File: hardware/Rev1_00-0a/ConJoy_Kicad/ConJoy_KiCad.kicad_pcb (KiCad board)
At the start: 2 copper layers, 40 x 59 mm, 20 parts, among them J1 SFV5R-2STBE1HLF, J11 5051102291, J8 0532610271, J9 0532610271

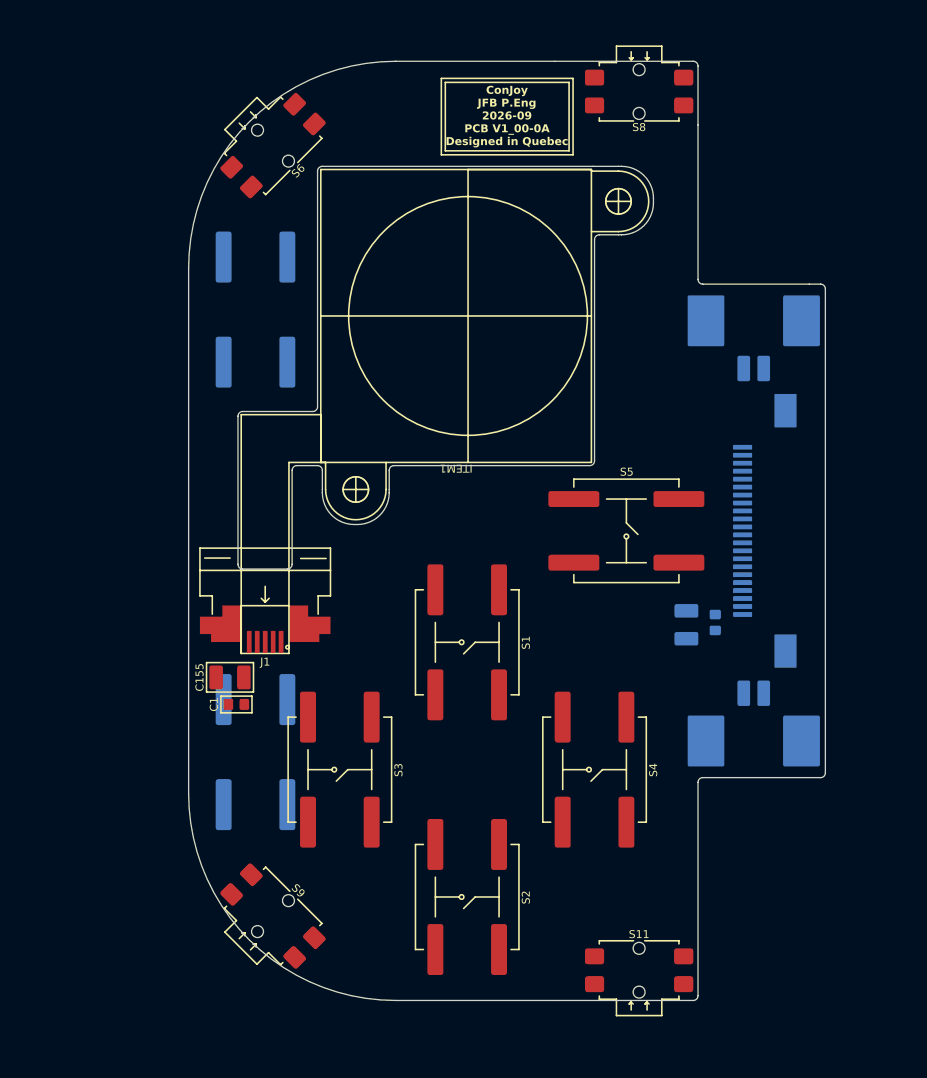
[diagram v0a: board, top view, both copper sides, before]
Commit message: Switch speaker pinout following footprint and 3d model review Add mounting holes
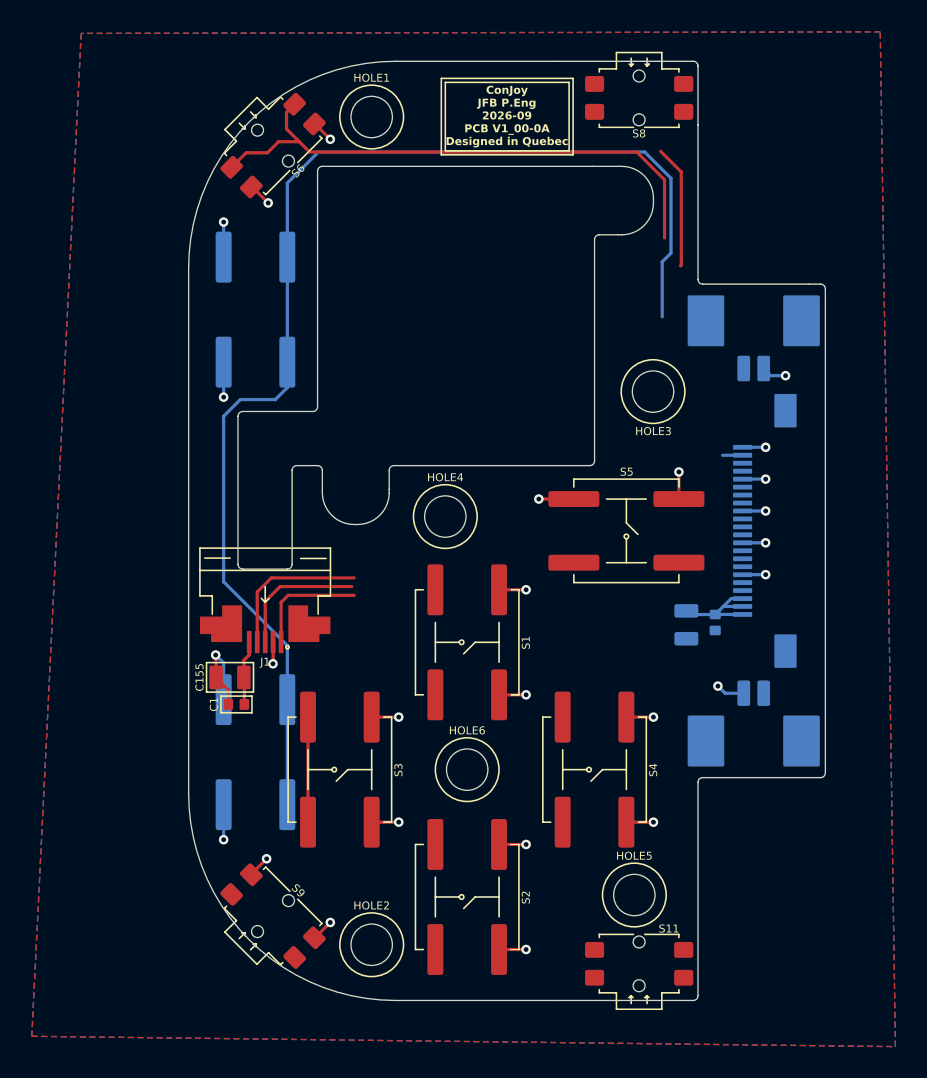
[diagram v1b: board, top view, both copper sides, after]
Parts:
- removed ITEM1: HallPi PCB FP, footprint:JoyCon_HallEffect_TMR
- added HOLE1: ~, footprint:NPTH_M2, F.Cu at (131.5, 95.5)
- added HOLE2: ~, footprint:NPTH_M2, F.Cu at (131.5, 147.5)
- added HOLE3: ~, footprint:NPTH_M2, F.Cu at (149.2, 112.8)
- added HOLE4: ~, footprint:NPTH_M2, F.Cu at (136.1, 120.6)
- added HOLE5: ~, footprint:NPTH_M2, F.Cu at (148.0, 144.4)
- added HOLE6: ~, footprint:NPTH_M2, F.Cu at (137.5, 136.5)
- moved S11 0.40 mm to (148.3, 148.7)
- moved S8 0.40 mm to (148.3, 94.3)
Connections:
- J1 pad 1: /L_THUMBST_X -> /L_R_THUMBST_X
- J1 pad 3: /L_THUMBST_SW -> /L_R_THUMBST_SW
- J1 pad 4: /L_THUMBST_Y -> /L_R_THUMBST_Y
- J8 pad 1: GND -> /L_R_SPKOUT
- J8 pad 2: /L_R_SPKOUT -> GND
- J9 pad 1: GND -> /L_R_SPKOUT
- J9 pad 2: /L_R_SPKOUT -> GND
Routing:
- net /L_R_L2_TRIG: track 0.00 -> 78.2 mm
- net GND: track 0.00 -> 48.2 mm, vias 0 -> 26
- net /L_R_L1_TRIG: track 0.00 -> 35.4 mm
- net 3V3: track 0.00 -> 11.0 mm
- net /L_R_THUMBST_Y: track 0.00 -> 9.60 mm
- net /L_HOME/R_EXTRA: track 0.00 -> 9.01 mm
- net /L_R_THUMBST_SW: track 0.00 -> 8.37 mm
- net /L_R_THUMBST_X: track 0.00 -> 7.27 mm
- net /L_DPAD_LEFT/R_BTN_X: track 0.00 -> 6.60 mm
- added copper zone on B.Cu, net GND
- added copper zone on F.Cu, net GND

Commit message: ConJoy mostly ready for alpha prototype. Confirm few other potential tweaks at 3d printing
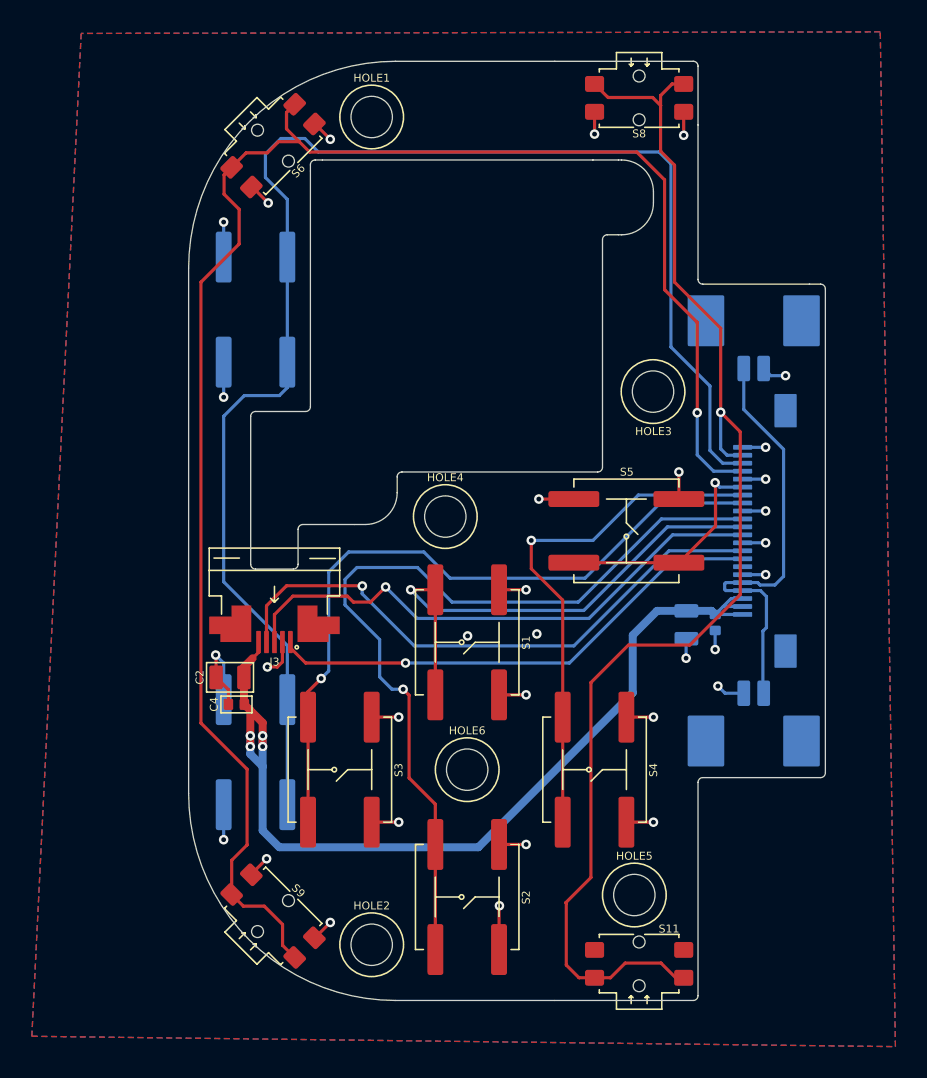
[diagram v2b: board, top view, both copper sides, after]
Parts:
- moved J3 0.58 mm to (125.4, 126.0)
- renumbered C156 to C1, C155 to C2, C2 to C3, C1 to C4, J9 to J1, J8 to J2, J1 to J3, J11 to J4
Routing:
- net /L_HOME/R_EXTRA: track 9.01 -> 82.3 mm, vias 0 -> 1
- net /L_R_L1_TRIG: track 35.4 -> 108.4 mm, vias 0 -> 1
- net /L_DPAD_DOWN/R_BTN_B: track 0.00 -> 54.4 mm, vias 0 -> 1
- net 3V3: track 11.0 -> 60.2 mm, vias 0 -> 4
- net /L_DPAD_LEFT/R_BTN_X: track 6.60 -> 45.4 mm, vias 0 -> 1
- net /L_DPAD_RIGHT/R_BTN_Y: track 0.00 -> 33.0 mm, vias 0 -> 1
- net /L_DPAD_UP/R_BTN_A: track 0.00 -> 31.7 mm, vias 0 -> 1
- net /L_R_SPKOUT: track 0.00 -> 27.5 mm
- net /L_R_THUMBST_Y: track 9.60 -> 37.0 mm, vias 0 -> 1
- net /L_R_THUMBST_SW: track 8.37 -> 35.2 mm, vias 0 -> 1
- net /L_R_THUMBST_X: track 7.27 -> 31.9 mm, vias 0 -> 1
- net /L_R_L2_TRIG: track 78.2 -> 94.0 mm
- net /L_START/R_SELECT: track 0.00 -> 14.4 mm, vias 0 -> 1
- net GND: track 48.2 -> 55.5 mm, vias 26 -> 32
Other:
- outline, holes or cut-outs redrawn

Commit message: Commit ConJoy design + output files (ready for manufacturing or REV 1.00-0A)
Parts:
- added D1: MMSZ5226B-7-F, footprint:SOD-123, B.Cu at (149.2, 128.3)
- added FID1: ~, footprint:FIDUCIAL, F.Cu at (148.3, 105.3)
- added FID2: ~, footprint:FIDUCIAL, B.Cu at (148.3, 105.3)
- added FID3: ~, footprint:FIDUCIAL, F.Cu at (129.0, 144.1)
- added FID4: ~, footprint:FIDUCIAL, B.Cu at (129.0, 144.1)
- added FID5: ~, footprint:FIDUCIAL, F.Cu at (142.7, 143.4)
- added FID6: ~, footprint:FIDUCIAL, B.Cu at (142.7, 143.4)
- HOLE1, HOLE2, HOLE3, HOLE4, HOLE5, HOLE6: moved to B.Cu
- turned HOLE1 to 180 degrees
- turned HOLE2 to 180 degrees
- turned HOLE3 to 180 degrees
- turned HOLE4 to 180 degrees
- turned HOLE5 to 180 degrees
- turned HOLE6 to 180 degrees
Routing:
- net GND: track 55.5 -> 60.3 mm, vias 32 -> 78
- net /L_R_THUMBST_Y: track 37.0 -> 36.1 mm
- net 3V3: track 60.2 -> 61.1 mm
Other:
- board text added: "PROD INFO"

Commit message: Add a lillllllll more clearance on inner cutout of ConJoy for Flat Flex cable of joystick
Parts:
- moved J3 0.51 mm to (125.3, 126.5)
- moved C2 0.30 mm to (122.6, 131.0)
- moved C4 0.30 mm to (123.0, 132.7)
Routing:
- net GND: track 60.3 -> 65.1 mm, vias 78 -> 75
- net /L_R_L1_TRIG: track 108.5 -> 112.3 mm
- net /L_R_THUMBST_X: track 31.9 -> 32.7 mm
- net /L_R_THUMBST_Y: track 36.1 -> 36.6 mm
- net /L_R_THUMBST_SW: track 35.2 -> 35.7 mm
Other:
- outline, holes or cut-outs redrawn

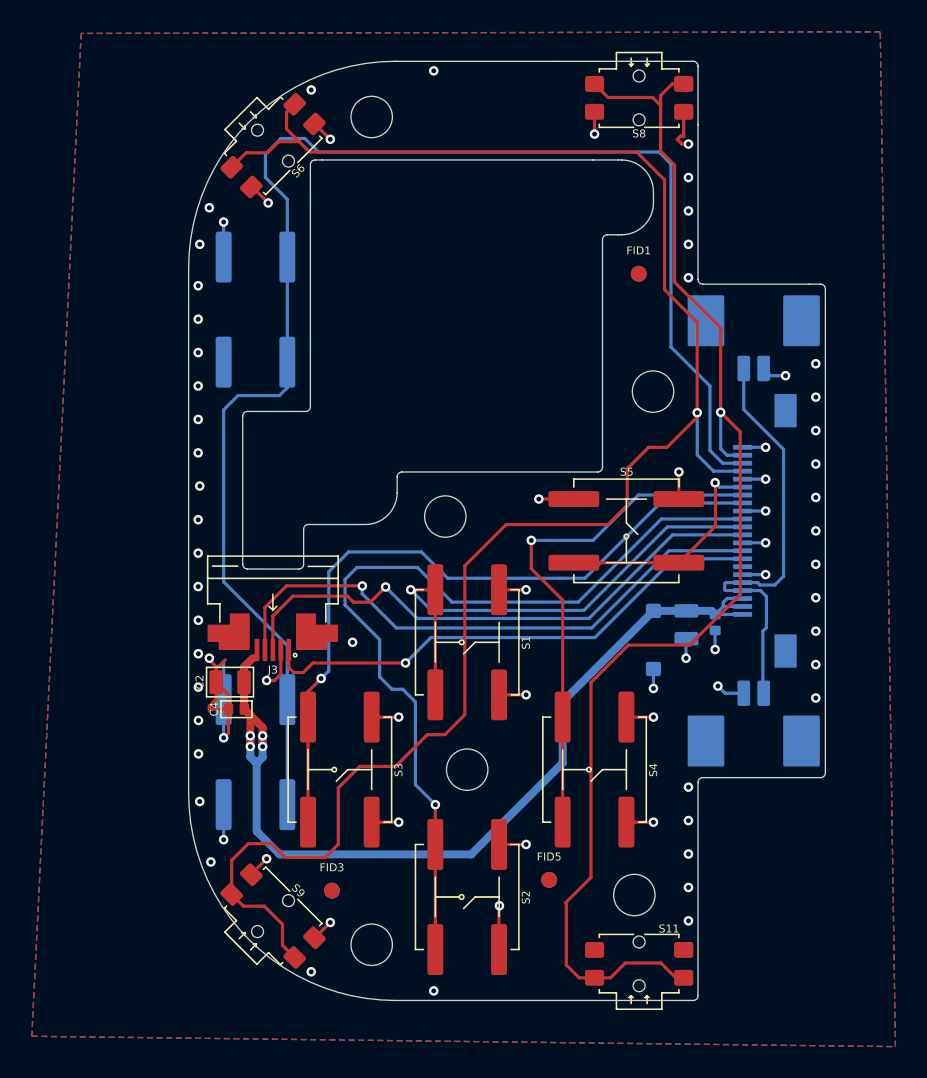
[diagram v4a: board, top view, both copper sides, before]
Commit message: Adjust mounting holes on ConJoy to ease case 3d modeling
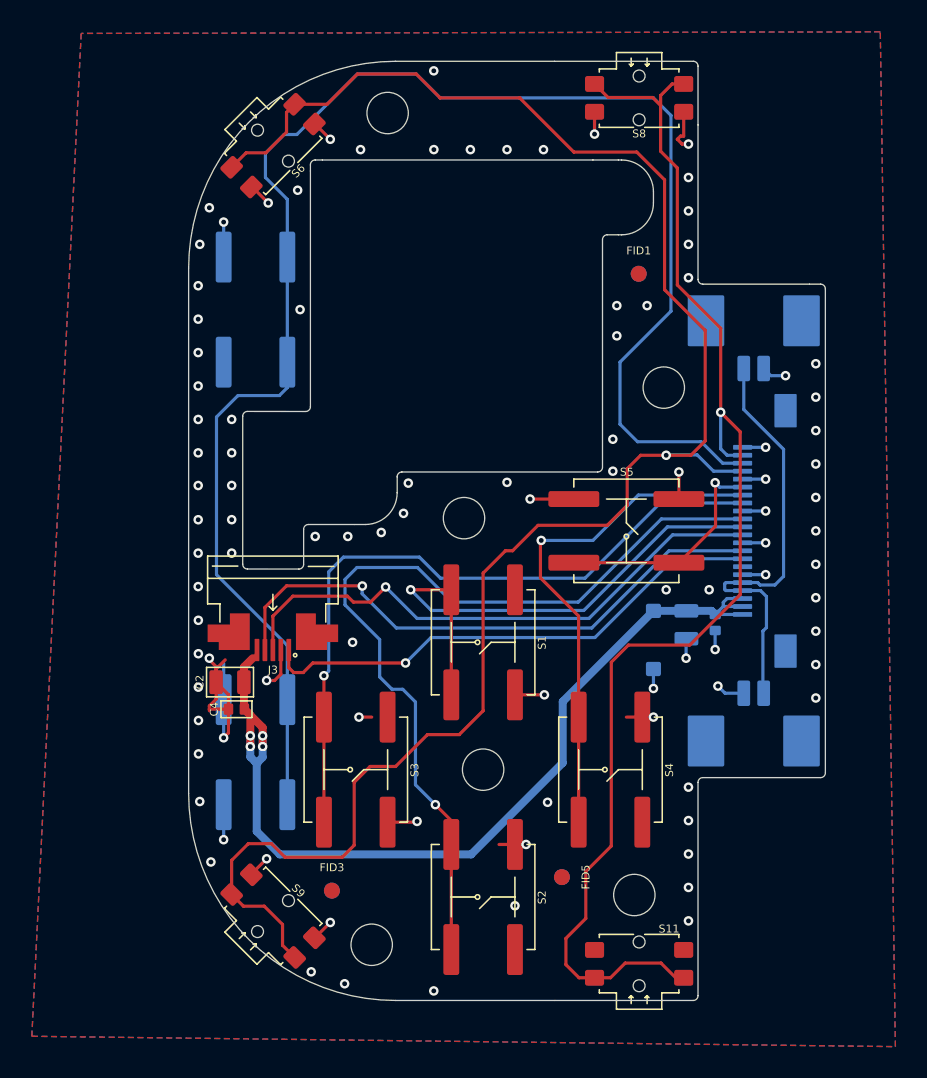
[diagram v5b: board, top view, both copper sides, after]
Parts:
- moved HOLE4 1.18 mm to (137.3, 120.7)
- moved HOLE1 1.03 mm to (132.5, 95.2)
- moved HOLE6 1.00 mm to (138.5, 136.5)
- moved S1 1.00 mm to (138.5, 128.5)
- moved S2 1.00 mm to (138.5, 144.5)
- moved S3 1.00 mm to (130.5, 136.5)
- moved S4 1.00 mm to (146.5, 136.5)
- moved FID5 0.82 mm to (143.4, 143.2)
- moved FID6 0.82 mm to (143.4, 143.2)
- moved HOLE3 0.72 mm to (149.8, 112.5)
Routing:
- net /L_R_L2_TRIG: track 94.2 -> 104.8 mm
- net GND: track 65.1 -> 59.0 mm, vias 75 -> 99
- net /L_R_L1_TRIG: track 112.3 -> 114.4 mm
- net /L_DPAD_UP/R_BTN_A: track 31.7 -> 32.7 mm
- net /L_DPAD_LEFT/R_BTN_X: track 45.4 -> 44.7 mm

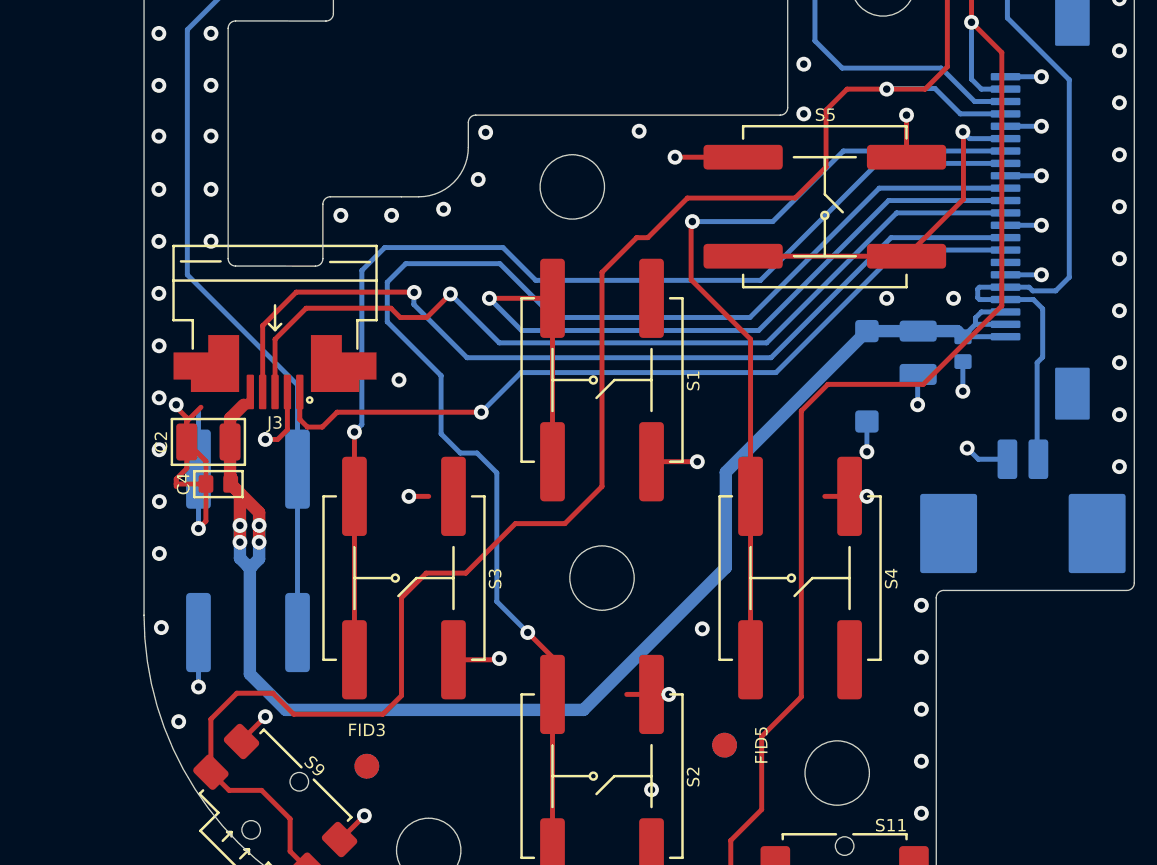
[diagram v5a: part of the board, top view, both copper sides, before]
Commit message: Move Joystick connector to bottom side of PCB Remove duplicate decoupling + bulk capacitors
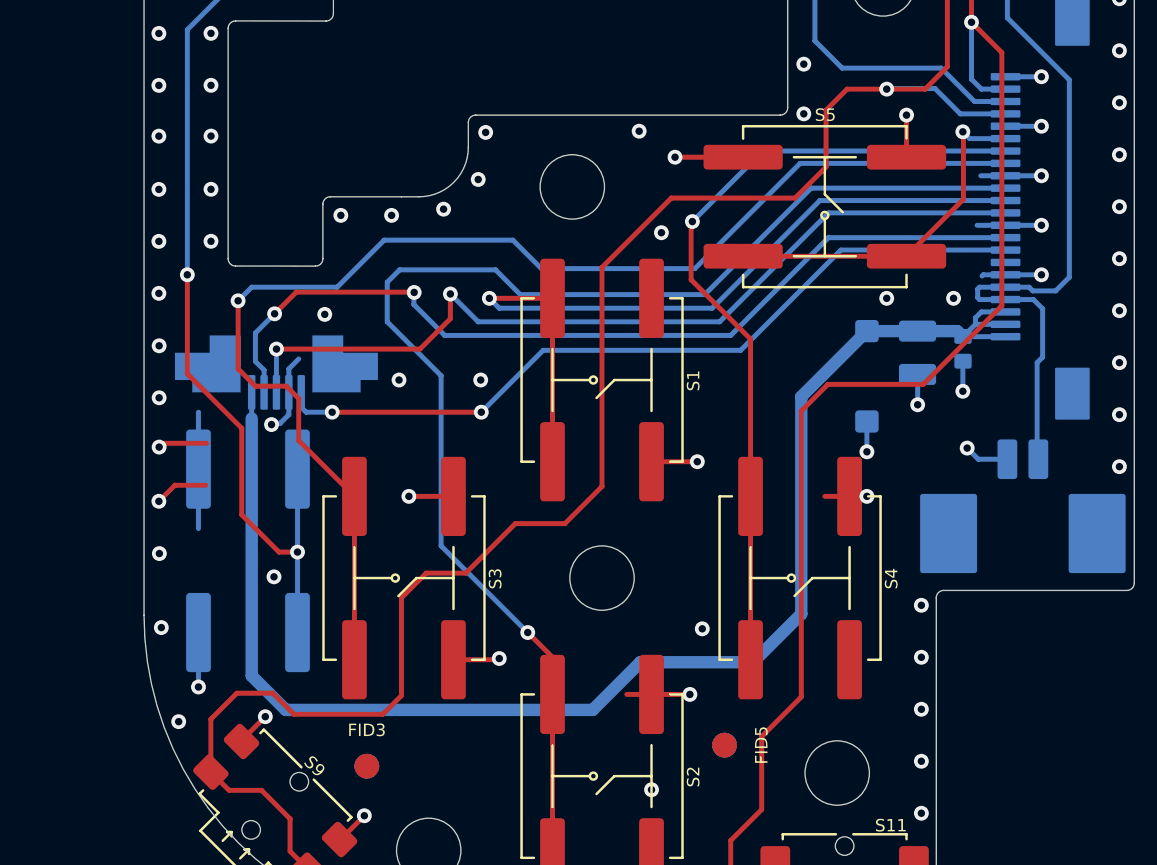
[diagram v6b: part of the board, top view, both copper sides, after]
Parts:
- removed C3, C4: 0.1u, footprint:CAP_NONPOL_0402
- C2: value 1u -> 0.1u; footprint footprint:CAP_NONPOL_0805 -> footprint:CAP_NONPOL_0402; moved to B.Cu
- J3: value SFV5R-2STBE1HLF -> SFV5R-1STE1HLF; footprint footprint:SFV5R-2ST -> footprint:SFV5R-1ST; moved to B.Cu
- moved C2 30.7 mm to (153.1, 127.2), turned to 90 degrees
- moved J3 0.06 mm to (125.3, 126.5), turned to 0 degrees
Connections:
- J3 pad 1: /L_R_THUMBST_X -> 3V3
- J3 pad 2: GND -> /L_R_THUMBST_Y
- J3 pad 4: /L_R_THUMBST_Y -> GND
- J3 pad 5: 3V3 -> /L_R_THUMBST_X
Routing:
- net /L_DPAD_LEFT/R_BTN_X: track 44.7 -> 51.4 mm
- net /L_R_L2_TRIG: track 104.8 -> 108.5 mm, vias 0 -> 2
- net 3V3: track 60.8 -> 57.5 mm, vias 4 -> 0
- net /L_DPAD_DOWN/R_BTN_B: track 54.8 -> 53.4 mm
- net GND: track 59.0 -> 58.0 mm, vias 99 -> 101
- net /L_R_THUMBST_X: track 32.7 -> 31.8 mm, vias 1 -> 2
- net /L_DPAD_UP/R_BTN_A: track 32.7 -> 32.0 mm
- net /L_R_THUMBST_SW: track 35.7 -> 35.0 mm, vias 1 -> 2
- net /L_R_THUMBST_Y: track 36.6 -> 36.2 mm, vias 1 -> 2

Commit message: Move Joycon connector slightly up to ease FFC / FPC connector handling and connecting
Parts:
- moved J3 2.00 mm to (125.3, 124.5)
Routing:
- net /L_DPAD_LEFT/R_BTN_X: track 51.4 -> 47.3 mm
- net 3V3: track 57.5 -> 59.5 mm
- net /L_R_THUMBST_SW: track 35.0 -> 36.5 mm
- net /L_R_THUMBST_Y: track 36.2 -> 34.9 mm
- net /L_R_THUMBST_X: track 31.8 -> 32.9 mm
- net GND: track 58.0 -> 57.9 mm, vias 101 -> 105
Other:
- outline, holes or cut-outs redrawn

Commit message: Update ConJoy L2 trigger (2-level trigger instead) Update ConJoy all output files accordingly
Work on Consolation preliminary placement
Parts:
- added C3: 1u, footprint:CAP_NONPOL_0805, B.Cu at (123.5, 129.4)
- S10, S7: value EVQ-Q2P03W -> TL1014BF160QG; footprint footprint:EVQQ2 -> footprint:TL1014B
- moved S7 10.4 mm to (125.3, 97.3), turned to 45 degrees
- moved S10 10.4 mm to (125.3, 145.7), turned to 135 degrees
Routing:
- net GND: track 57.9 -> 50.7 mm, vias 105 -> 121
- net /L_R_L2_TRIG: track 108.5 -> 114.1 mm
- net /L_R_L1_TRIG: track 114.5 -> 115.1 mm
- net 3V3: track 59.5 -> 59.0 mm
